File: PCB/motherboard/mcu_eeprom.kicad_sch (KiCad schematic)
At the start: 1 part, among them U5 NUCLEO-L432KC

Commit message: test kicad collab
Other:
- moved on the sheet: U5A, U5B

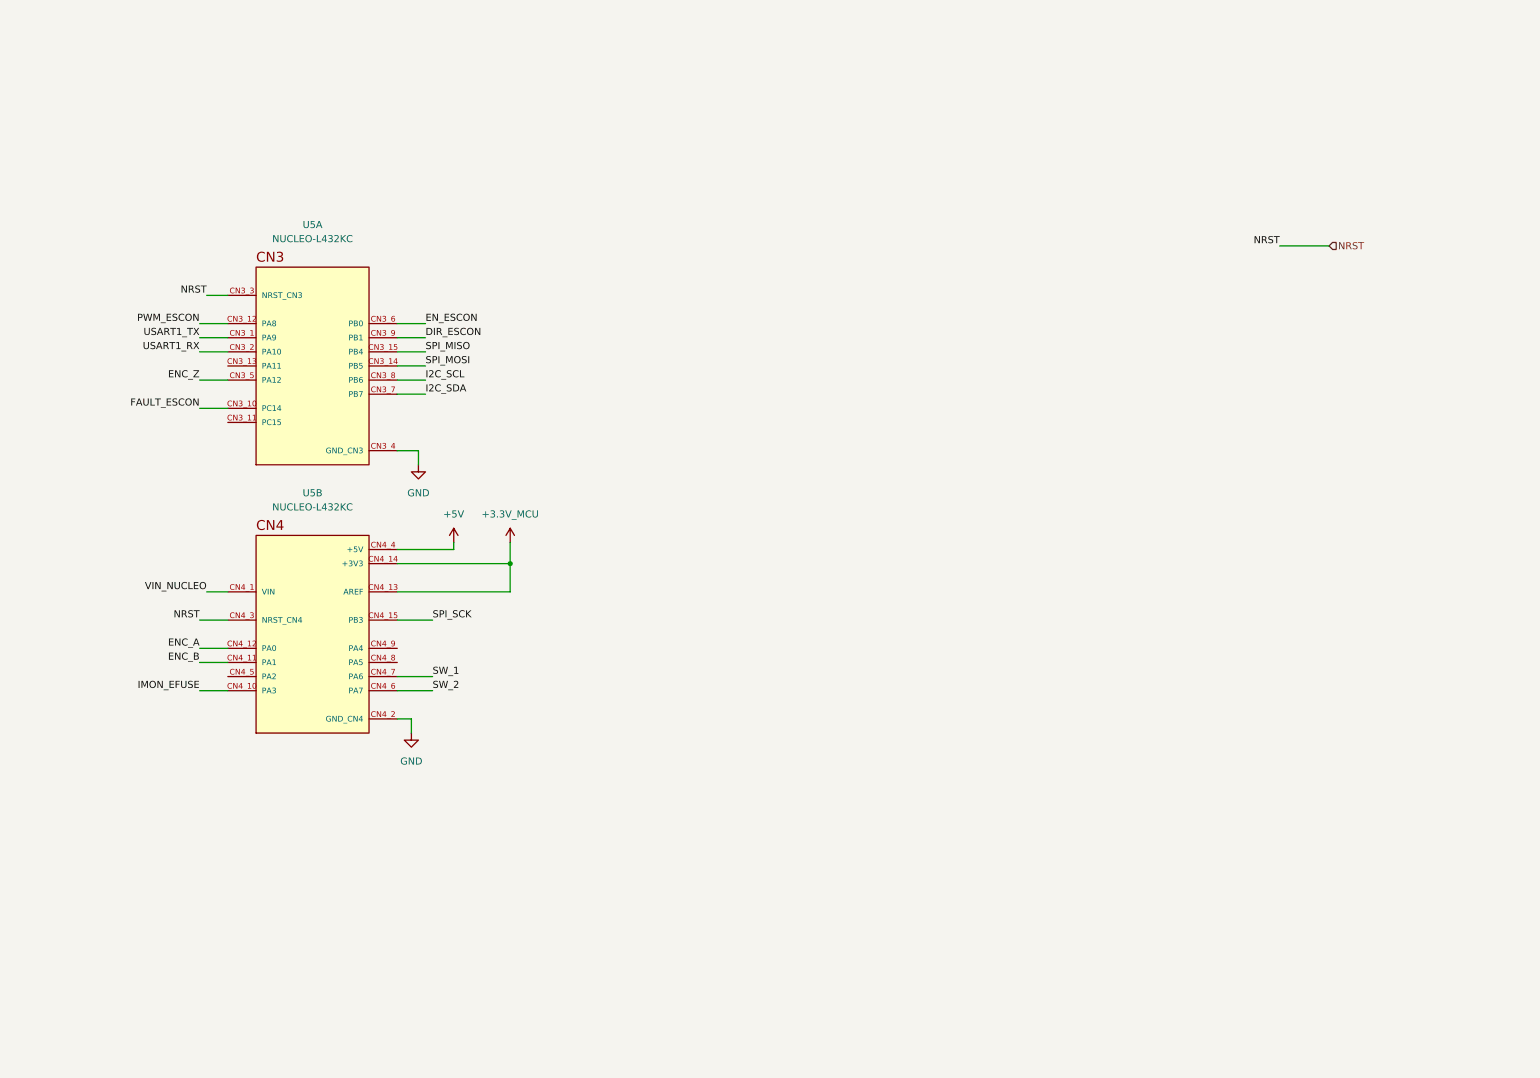
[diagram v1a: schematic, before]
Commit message: added hierrcical labels mcu, added filters for escon + labels
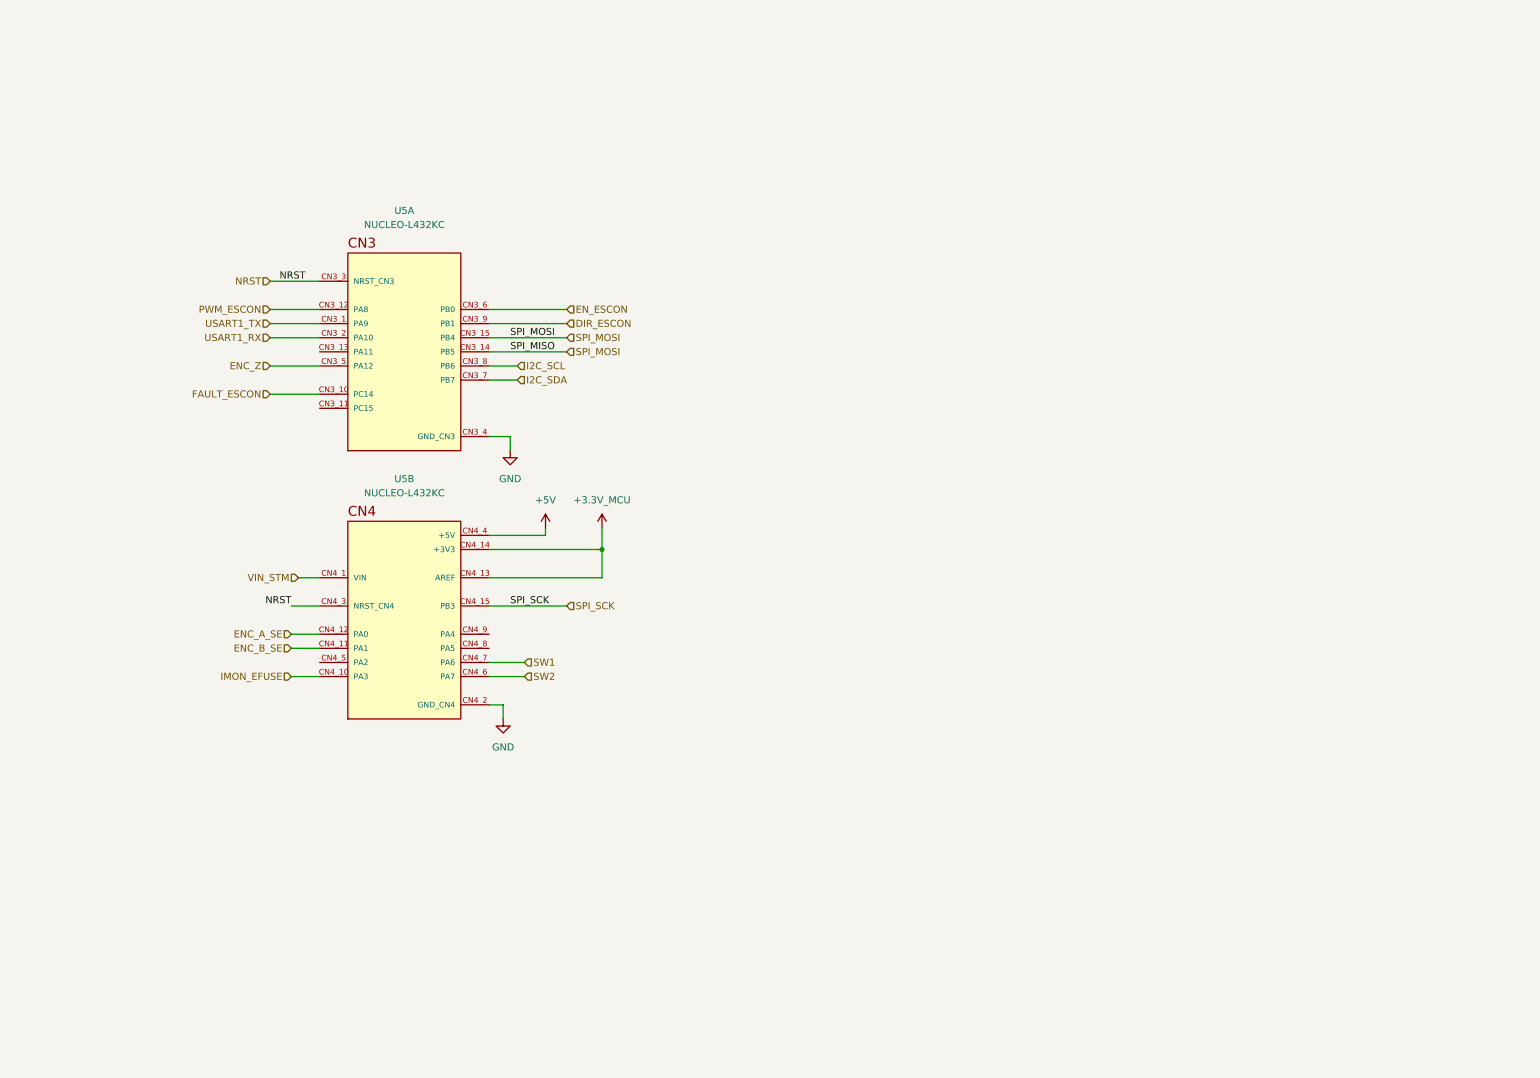
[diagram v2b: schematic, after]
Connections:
- net SPI_MISO is gone; now on net SPI_MOSI: U5.CN3_15 (PB4)
- net ENC_A renamed ENC_A_SE
- net ENC_B renamed ENC_B_SE
- net SW_1 renamed SW1
- net SW_2 renamed SW2
- net VIN_NUCLEO renamed VIN_STM
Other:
- moved on the sheet: U5A, U5B

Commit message: reverse current protection on ESCON+others
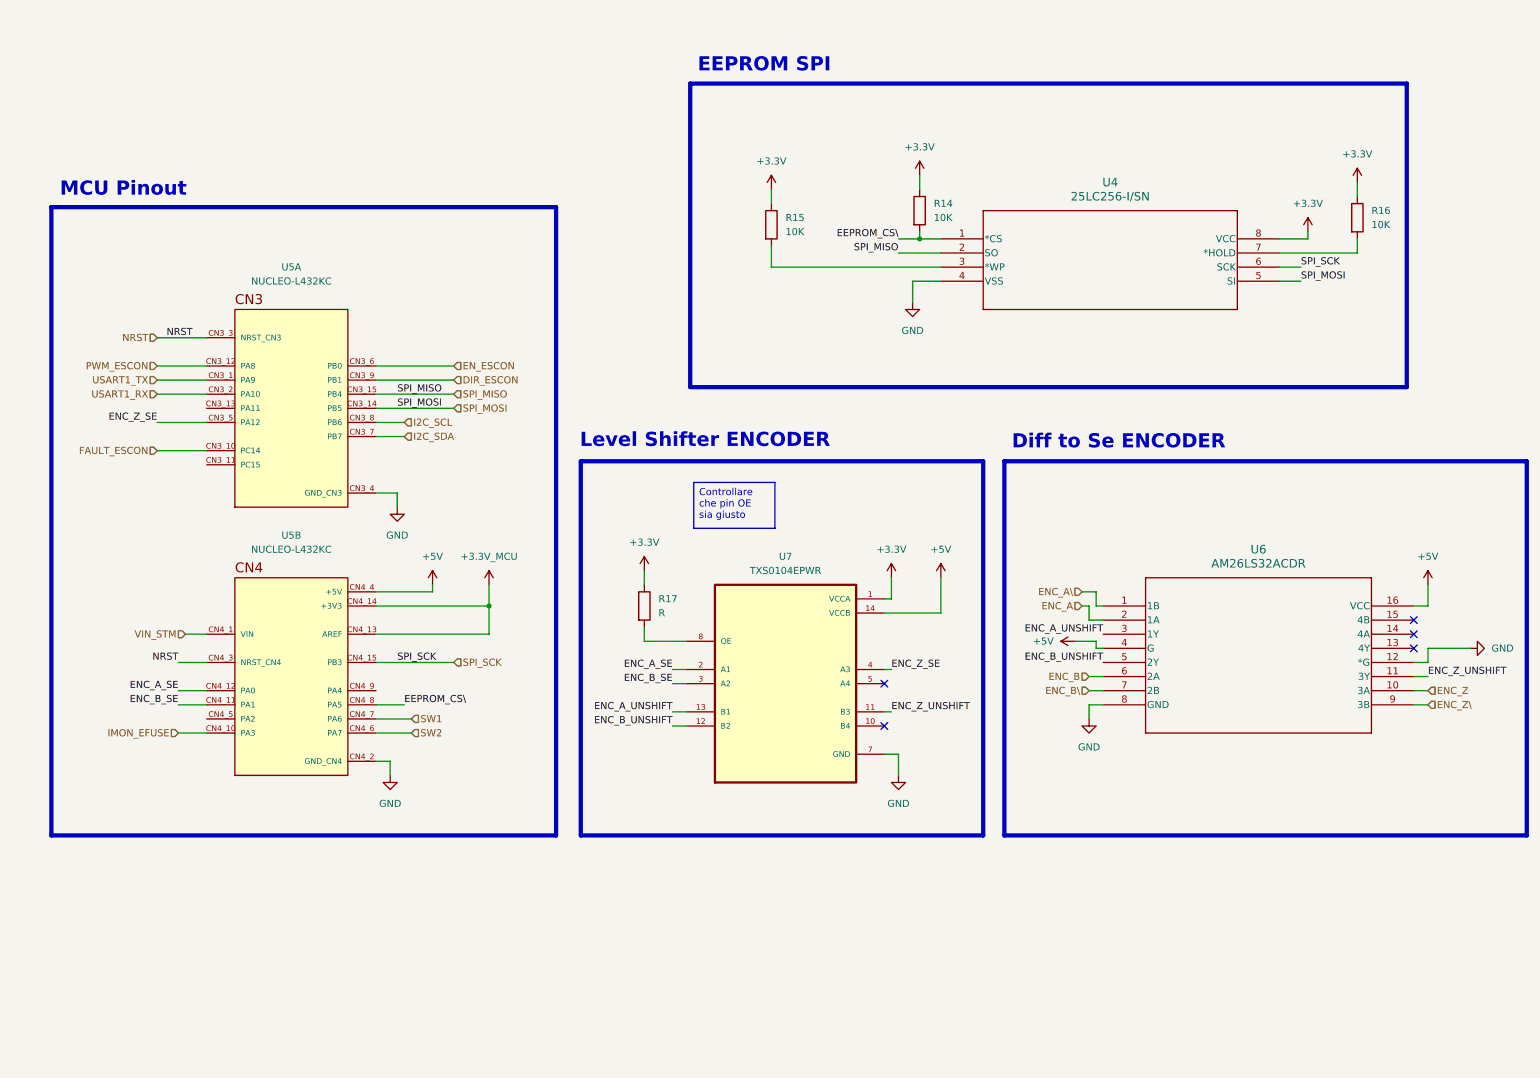
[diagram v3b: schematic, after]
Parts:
- added R14, R15, R16: 10K, symbol Device:R
- added R17: R, symbol Device:R
- added U4: 25LC256-I/SN, SOIC8-N_MC_MCH, symbol 25LC256-ISN:25LC256-I_SN
- added U6: AM26LS32ACDR, D16, symbol AM26LS32ACDR:AM26LS32ACDR
- added U7: TXS0104EPWR, TXS0104EPWR:SOP65P640X120-14N, symbol TXS0104EPWR:TXS0104EPWR
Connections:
- net +5V: now also U6.16 (VCC), U6.4 (G), U7.14 (VCCB)
- net ENC_A_SE: now also U7.2 (A1)
- net ENC_B_SE: now also U7.3 (A2)
- net ENC_Z: now also U6.10 (3A); no longer U5.CN3_5 (PA12)
- net GND: now also U4.4 (VSS), U6.12 (*G), U6.8 (GND), U7.7 (GND)
- net SPI_MOSI: now also U4.5 (SI); no longer U5.CN3_15 (PB4)
- net SPI_SCK: now also U4.6 (SCK)
- net EEPROM_CS\: now reaches U5.CN4_8 (PA5)
- net EEPROM_CS\: now also R14.2, U4.1 (*CS)
- new net: R17.2, U7.8 (OE)
- new net: R15.2, U4.3 (*WP)
- new net: R16.2, U4.7 (*HOLD)
- new net +3.3V: R14.1, R15.1, R16.1, R17.1, U4.8 (VCC), U7.1 (VCCA)
- new net ENC_A: U6.2 (1A)
- new net ENC_A\: U6.1 (1B)
- new net ENC_A_UNSHIFT: U6.3 (1Y), U7.13 (B1)
- new net ENC_B: U6.6 (2A)
- new net ENC_B\: U6.7 (2B)
- new net ENC_B_UNSHIFT: U6.5 (2Y), U7.12 (B2)
- new net ENC_Z\: U6.9 (3B)
- new net ENC_Z_SE: U5.CN3_5 (PA12), U7.4 (A3)
- new net ENC_Z_UNSHIFT: U6.11 (3Y), U7.11 (B3)
- new net SPI_MISO: U4.2 (SO), U5.CN3_15 (PB4)
- no-connect marks 0 -> 5
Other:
- note added: "Diff to Se ENCODER"
- note added: "EEPROM SPI"
- note added: "Level Shifter ENCODER"
- note added: "MCU Pinout"
- moved on the sheet: U5A, U5B

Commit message: collegamenti tra blocchi schematico, sistemati connettori,finita la parte di shunt monitor per back EMF escon, aggiunti status LED, aggiunti bulk cap su alimentazione+altre modifiche
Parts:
- R17: value R -> 10k
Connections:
- net PC15: now reaches U5.CN3_11 (PC15)
- net PA11: now reaches U5.CN3_13 (PA11)
- net PA2: now reaches U5.CN4_5 (PA2)
- net PA4: now reaches U5.CN4_9 (PA4)
- net NRST: no longer names the net of U5.CN3_3 (NRST_CN3)
- net NRST: no longer U5.CN4_3 (NRST_CN4)
- net VIN_STM: no longer names the net of U5.CN4_1 (VIN)
- no-connect marks 5 -> 8

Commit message: schematics need only sizing
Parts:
- added Q3: NMOS, symbol Simulation_SPICE:NMOS
- added R31: 10k, Resistor_SMD:R_1206_3216Metric_Pad1.30x1.75mm_HandSolder, symbol Device:R
- R19: renamed from R17; footprint (none) -> Resistor_SMD:R_1206_3216Metric_Pad1.30x1.75mm_HandSolder
- R20: renamed from R15; footprint (none) -> Resistor_SMD:R_1206_3216Metric_Pad1.30x1.75mm_HandSolder
- R21: renamed from R14; footprint (none) -> Resistor_SMD:R_1206_3216Metric_Pad1.30x1.75mm_HandSolder
- R25: renamed from R16; footprint (none) -> Resistor_SMD:R_1206_3216Metric_Pad1.30x1.75mm_HandSolder
- U4: renamed from U5; footprint NUCLEO-L432KC:MODULE_NUCLEO-L432KC -> NUCLEO_L432KC:MODULE_NUCLEO-L432KC
- U7: renamed from U4; footprint SOIC8-N_MC_MCH -> 25LC256-ISN:SOIC8-N_MC_MCH
- U8: renamed from U6; footprint D16 -> AM26LS32ACDR:D16
- renumbered U7 to U5
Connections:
- net GND: now also Q3.3 (S), R31.2
- net PA2 renamed HEATER
- net HEATER: now also Q3.2 (G), R31.1
- new net HEAT_GND: Q3.1 (D)
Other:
- note added: "HEATER ACTUATOR"
- moved on the sheet: U4A, U4B

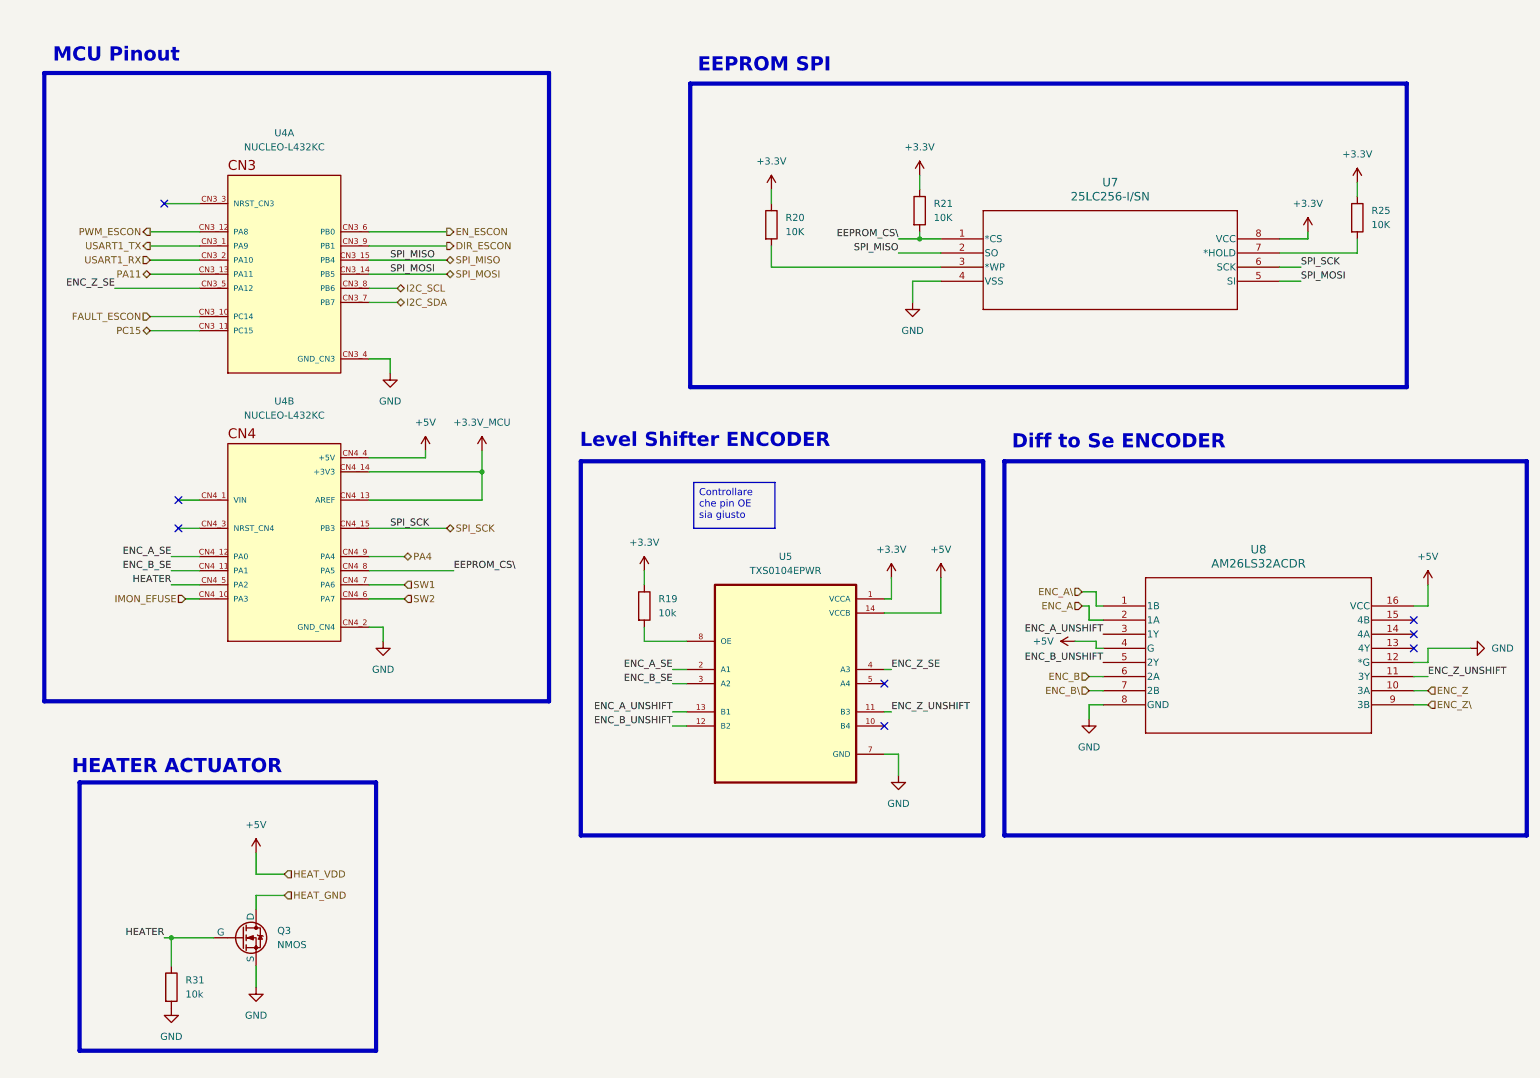
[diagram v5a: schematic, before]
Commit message: sizing schematics done
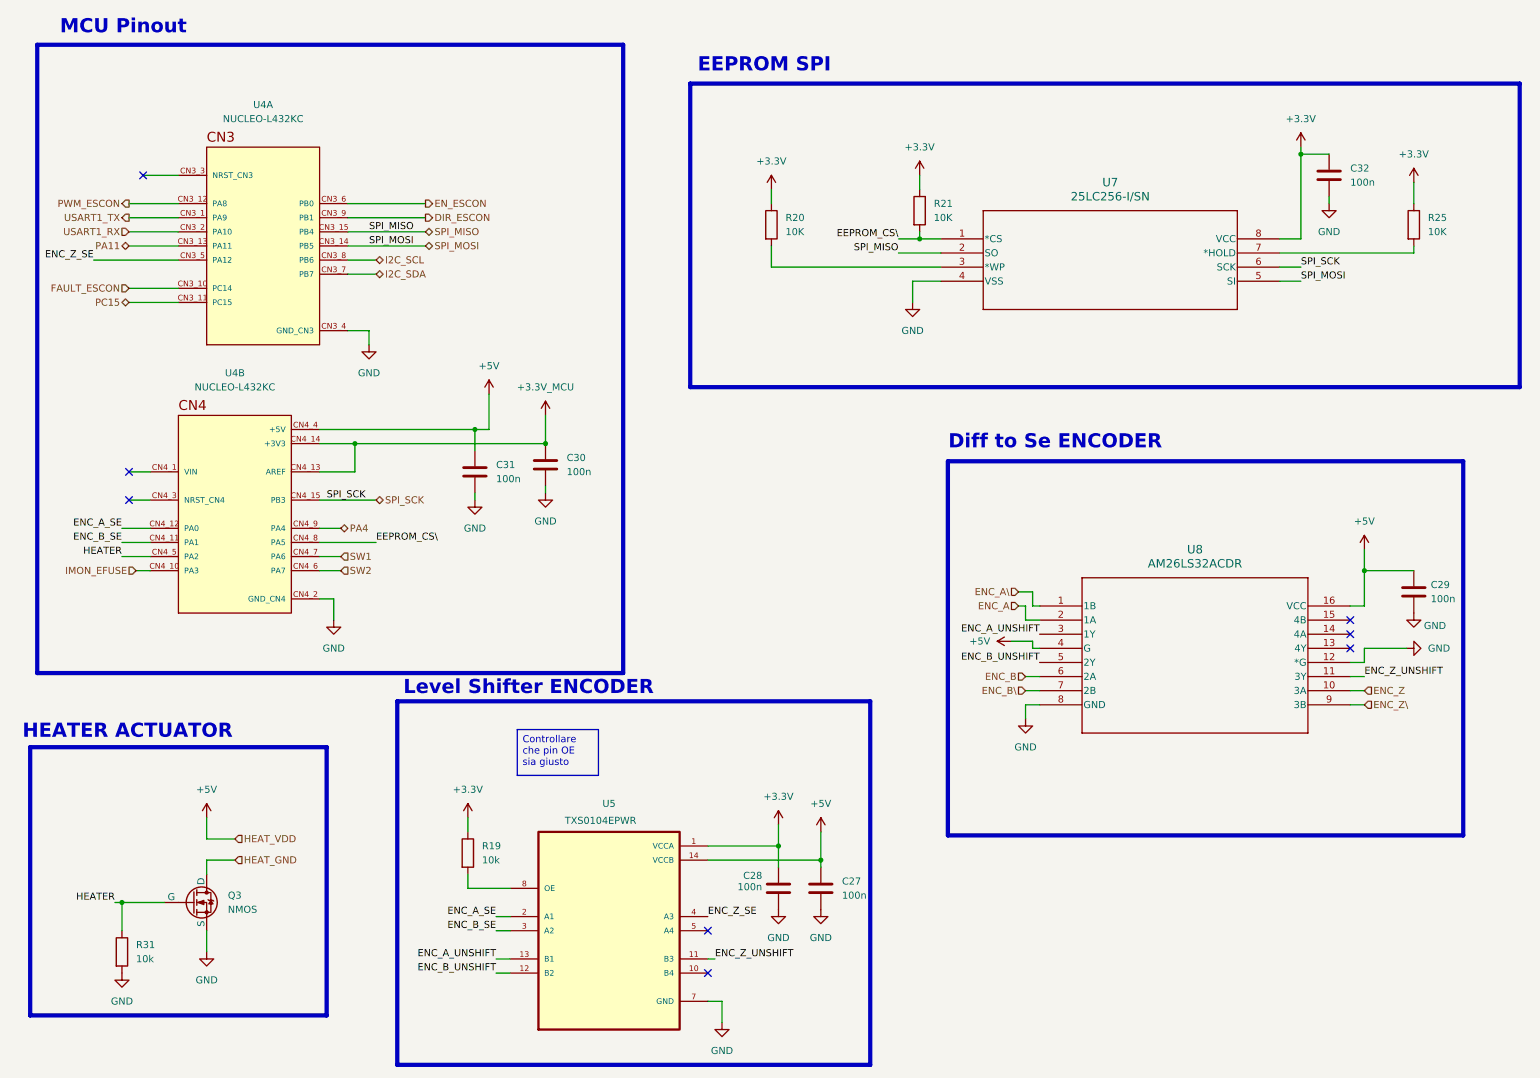
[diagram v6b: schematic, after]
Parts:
- added C27, C28, C29, C30, C31, C32: 100n, Capacitor_SMD:C_1206_3216Metric_Pad1.33x1.80mm_HandSolder, symbol Device:C
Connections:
- net +3.3V: now also C28.1, C32.1
- net +3.3V_MCU: now also C30.1
- net +5V: now also C27.1, C29.1, C31.1
- net GND: now also C27.2, C28.2, C29.2, C30.2, C31.2, C32.2
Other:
- moved on the sheet: Q3, R19, R25, R31, U4A, U4B, U5, U8

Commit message: added last footprint on sch
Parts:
- Q3: footprint (none) -> transistors:SOT-23-3_L2.9-W1.3-P1.90-LS2.4-BR
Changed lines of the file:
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@@
 			)
 		)
-		(property "Footprint" ""
+		(property "Footprint" "transistors:SOT-23-3_L2.9-W1.3-P1.90-LS2.4-BR"
 			(at 46.99 166.37 0)
 			(hide yes)

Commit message: pcb layout
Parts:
- added D7: LED_YELLOW, LED_SMD:LED_1206_3216Metric_Pad1.42x1.75mm_HandSolder, symbol Device:LED
- added R32: 1k, Resistor_SMD:R_1206_3216Metric_Pad1.30x1.75mm_HandSolder, symbol Device:R
- C27, C28, C29, C30, C31, C32: VRATE (none) -> 16
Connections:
- net +5V: now also R32.1
- net HEAT_GND: now also D7.1 (K)
- new net: D7.2 (A), R32.2
- no-connect marks 8 -> 10
